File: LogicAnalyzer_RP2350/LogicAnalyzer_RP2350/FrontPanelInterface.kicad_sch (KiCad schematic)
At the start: 1 part, among them J1 874370843

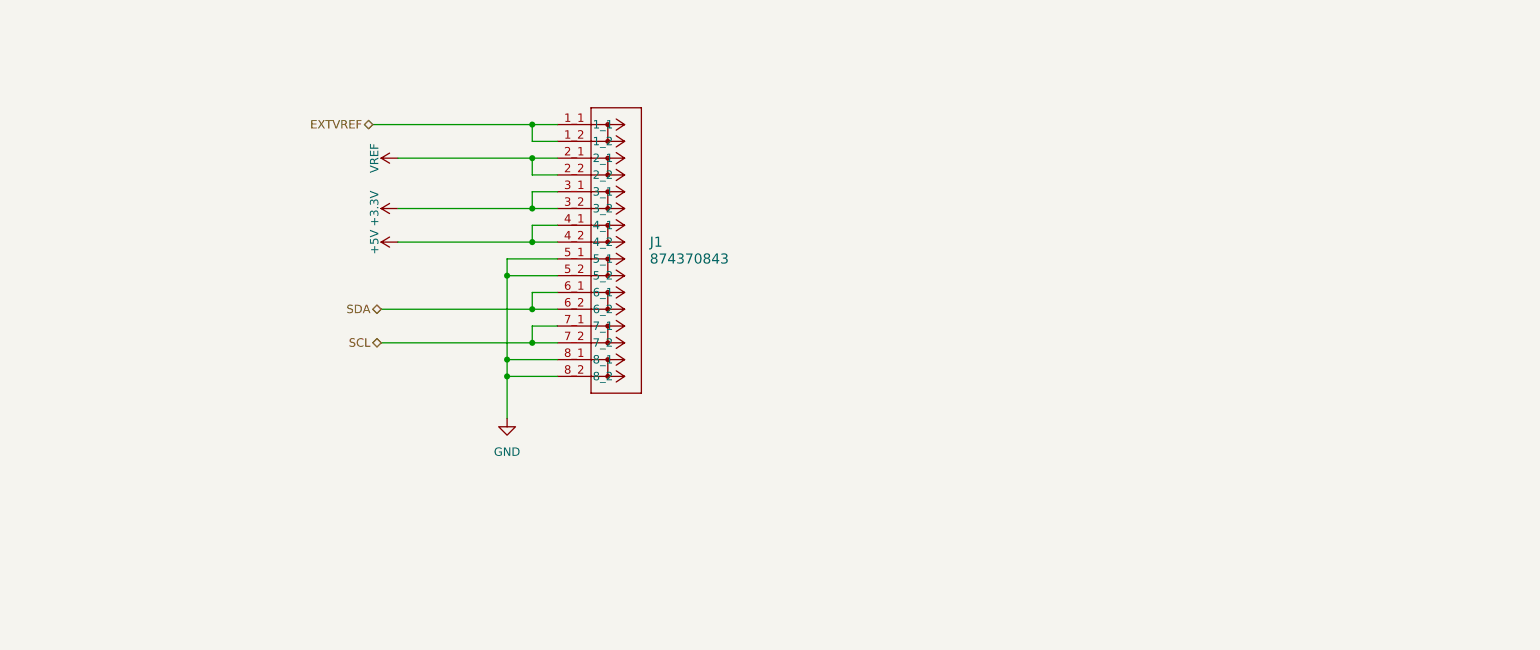
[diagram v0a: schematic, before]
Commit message: Added VMON Micro
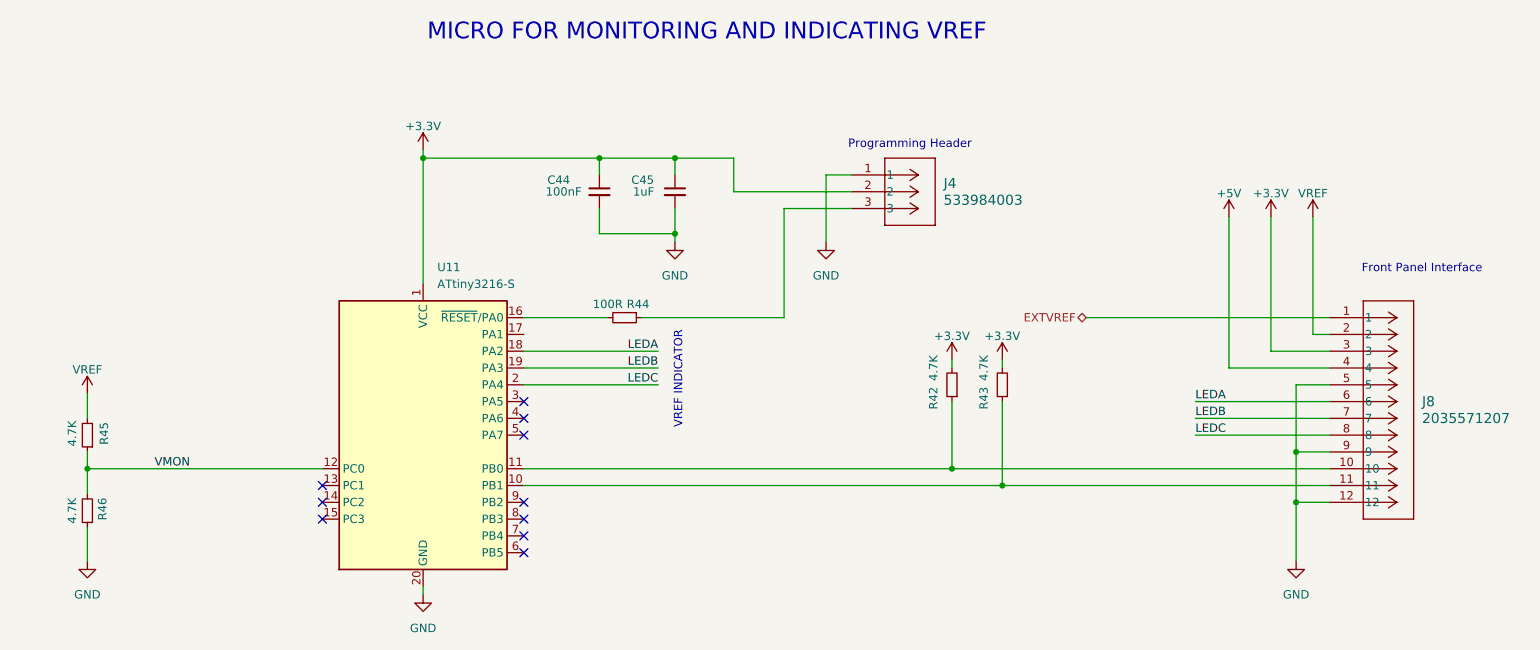
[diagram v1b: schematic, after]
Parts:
- removed J1: 874370843, CONN_874370231-SD_08_MOL, symbol Molex-874370843:874370843
- added C44: 100nF, Capacitor_SMD:C_0603_1608Metric_Pad1.08x0.95mm_HandSolder, symbol Device:C_Small
- added C45: 1uF, Capacitor_SMD:C_0603_1608Metric_Pad1.08x0.95mm_HandSolder, symbol Device:C_Small
- added J4: 533984003, CONN_533980002-SD_03_MOL, symbol Molex-533984003:533984003
- added J8: 2035571207, CONN_2035570000-SD_12_MOL, symbol Molex-2035571207:2035571207
- added R42, R43, R45, R46: 4.7K, Resistor_SMD:R_0603_1608Metric_Pad0.98x0.95mm_HandSolder, symbol Device:R_Small
- added R44: 100R, Resistor_SMD:R_0603_1608Metric_Pad0.98x0.95mm_HandSolder, symbol Device:R_Small
- added U11: ATtiny3216-S, Package_SO:SOIC-20W_7.5x12.8mm_P1.27mm, symbol MCU_Microchip_ATtiny:ATtiny3216-S
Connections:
- net +3.3V: now also C44.1, C45.1, J4.2, J8.3, R42.2, R43.2, U11.1 (VCC)
- net +5V: now also J8.4
- net EXTVREF: now also J8.1
- net GND: now also C44.2, C45.2, J4.1, J8.12, J8.5, J8.9, R46.1, U11.20 (GND)
- net VREF: now also J8.2, R45.2
- new net: J4.3, R44.1
- new net: R44.2, U11.16 (~{RESET}/PA0)
- new net: J8.11, R43.1, U11.10 (PB1)
- new net: J8.10, R42.1, U11.11 (PB0)
- new net LEDA: J8.6, U11.18 (PA2)
- new net LEDB: J8.7, U11.19 (PA3)
- new net LEDC: J8.8, U11.2 (PA4)
- new net VMON: R45.1, R46.2, U11.12 (PC0)
- no-connect marks 0 -> 10
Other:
- note added: "Front Panel Interface"
- note added: "MICRO FOR MONITORING AND INDICATING VREF"
- note added: "Programming Header"
- note added: "VREF INDICATOR"

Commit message: Clearing UP ERC Errors and Warnings
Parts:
- J4: footprint CONN_533980002-SD_03_MOL -> Molex-533984003:CONN_533980002-SD_03_MOL
- J8: footprint CONN_2035570000-SD_12_MOL -> Molex-2035571207:CONN_2035570000-SD_12_MOL
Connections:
- no-connect marks 10 -> 11
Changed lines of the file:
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@@
+	)
+	(no_connect
+		(at 110.49 91.44)
 	)
 	(no_connect
@@
 			)
 			(justify left bottom)
+		)
+	)
+	(hierarchical_label "VREF"
+		(shape output)
+		(at 44.45 100.33 90)
+		(effects
+			(font
+				(size 1.27 1.27)
+			)
+			(justify left)
+		)
+	)
+	(hierarchical_label "VREF"
+		(shape output)
+		(at 229.87 73.66 90)
+		(effects
+			(font
+				(size 1.27 1.27)
+			)
+			(justify left)
 		)
 	)
@@
 			)
 		)
-		(property "Footprint" "CONN_533980002-SD_03_MOL"
+		(property "Footprint" "Molex-533984003:CONN_533980002-SD_03_MOL"
 			(at 160.02 67.31 0)
 			(hide yes)
@@
 			)
 		)
-		(property "Footprint" "CONN_2035570000-SD_12_MOL"
+		(property "Footprint" "Molex-2035571207:CONN_2035570000-SD_12_MOL"
 			(at 232.41 88.9 0)
 			(hide yes)
@@
 	)
 	(symbol
-		(lib_id "power:+2V5")
-		(at 229.87 73.66 0)
-		(unit 1)
-		(body_style 1)
-		(exclude_from_sim no)
-		(in_bom yes)
-		(on_board yes)
-		(in_pos_files yes)
-		(dnp no)
-		(property "Reference" "#PWR0101"
-			(at 229.87 77.47 0)
-			(hide yes)
-			(show_name no)
-			(do_not_autoplace no)
-			(effects
-				(font
-					(size 1.27 1.27)
-				)
-			)
-		)
-		(property "Value" "VREF"
-			(at 229.87 70.104 0)
-			(show_name no)
-			(do_not_autoplace no)
-			(effects
-				(font
-					(size 1.27 1.27)
-				)
-			)
-		)
-		(property "Footprint" ""
-			(at 229.87 73.66 0)
-			(hide yes)
-			(show_name no)
-			(do_not_autoplace no)
-			(effects
-				(font
-					(size 1.27 1.27)
-				)
-			)
-		)
-		(property "Datasheet" ""
-			(at 229.87 73.66 0)
-			(hide yes)
-			(show_name no)
-			(do_not_autoplace no)
-			(effects
-				(font
-					(size 1.27 1.27)
-				)
-			)
-		)
-		(property "Description" "Power symbol creates a global label with name \"+2V5\""
-			(at 229.87 73.66 0)
-			(hide yes)
-			(show_name no)
-			(do_not_autoplace no)
-			(effects
-				(font
-					(size 1.27 1.27)
-				)
-			)
-		)
-		(pin "1"
-		)
-		(instances
-			(project "LogicAnalyzer_RP2350"
-				(path "/d75f24d0-99d8-459e-8e7b-473191ec3959/68c34580-4572-474c-bc8b-c0b67926a418"
-					(reference "#PWR0101")
-					(unit 1)
-				)
-			)
-		)
-	)
-	(symbol
 		(lib_id "Device:R_Small")
 		(at 44.45 106.68 180)
@@
 					(unit 1)
 				)
-			)
-		)
-	)
-	(symbol
-		(lib_id "power:+2V5")
-		(at 44.45 100.33 0)
-		(unit 1)
-		(body_style 1)
-		(exclude_from_sim no)
-		(in_bom yes)
-		(on_board yes)
-		(in_pos_files yes)
-		(dnp no)
-		(property "Reference" "#PWR0100"
-			(at 44.45 104.14 0)
-			(hide yes)
-			(show_name no)
-			(do_not_autoplace no)
-			(effects
-				(font
-					(size 1.27 1.27)
-				)
-			)
-		)
-		(property "Value" "VREF"
-			(at 44.45 96.774 0)
-			(show_name no)
-			(do_not_autoplace no)
-			(effects
-				(font
-					(size 1.27 1.27)
-				)
-			)
-		)
-		(property "Footprint" ""
-			(at 44.45 100.33 0)
-			(hide yes)
-			(show_name no)
-			(do_not_autoplace no)
-			(effects
-				(font
-					(size 1.27 1.27)
-				)
-			)
-		)
-		(property "Datasheet" ""
-			(at 44.45 100.33 0)
-			(hide yes)
-			(show_name no)
-			(do_not_autoplace no)
-			(effects
-				(font
-					(size 1.27 1.27)
-				)
-			)
-		)
-		(property "Description" "Power symbol creates a global label with name \"+2V5\""
-			(at 44.45 100.33 0)
-			(hide yes)
-			(show_name no)
-			(do_not_autoplace no)
-			(effects
-				(font
-					(size 1.27 1.27)
-				)
-			)
-		)
-		(pin "1"
-		)
-		(instances
-			(project "LogicAnalyzer_RP2350"
-				(path "/d75f24d0-99d8-459e-8e7b-473191ec3959/68c34580-4572-474c-bc8b-c0b67926a418"
-					(reference "#PWR0100")
-					(unit 1)
-				)

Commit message: Net Classes Added
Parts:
- renumbered C44 to C45, C45 to C46, J4 to J7, R44 to R47, R42 to R48, R43 to R49
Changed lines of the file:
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@@
 		(in_pos_files yes)
 		(dnp no)
-		(property "Reference" "#PWR096"
+		(property "Reference" "#PWR080"
 			(at 95.25 67.31 0)
 			(hide yes)
@@
 			(project "LogicAnalyzer_RP2350"
 				(path "/d75f24d0-99d8-459e-8e7b-473191ec3959/68c34580-4572-474c-bc8b-c0b67926a418"
-					(reference "#PWR096")
+					(reference "#PWR080")
 					(unit 1)
 				)
@@
 		(in_pos_files yes)
 		(dnp no)
-		(property "Reference" "#PWR0103"
+		(property "Reference" "#PWR086"
 			(at 217.17 77.47 0)
 			(hide yes)
@@
 			(project "LogicAnalyzer_RP2350"
 				(path "/d75f24d0-99d8-459e-8e7b-473191ec3959/68c34580-4572-474c-bc8b-c0b67926a418"
-					(reference "#PWR0103")
+					(reference "#PWR086")
 					(unit 1)
 				)
@@
 		(dnp no)
 		(fields_autoplaced yes)
-		(property "Reference" "#PWR087"
+		(property "Reference" "#PWR082"
 			(at 133.35 83.82 0)
 			(hide yes)
@@
 			(project "LogicAnalyzer_RP2350"
 				(path "/d75f24d0-99d8-459e-8e7b-473191ec3959/68c34580-4572-474c-bc8b-c0b67926a418"
-					(reference "#PWR087")
+					(reference "#PWR082")
 					(unit 1)
 				)
@@
 		(dnp no)
 		(fields_autoplaced yes)
-		(property "Reference" "#PWR088"
+		(property "Reference" "#PWR083"
 			(at 156.21 83.82 0)
 			(hide yes)
@@
 			(project "LogicAnalyzer_RP2350"
 				(path "/d75f24d0-99d8-459e-8e7b-473191ec3959/68c34580-4572-474c-bc8b-c0b67926a418"
-					(reference "#PWR088")
+					(reference "#PWR083")
 					(unit 1)
 				)
@@
 		(dnp no)
 		(fields_autoplaced yes)
-		(property "Reference" "#PWR0104"
+		(property "Reference" "#PWR088"
 			(at 227.33 132.08 0)
 			(hide yes)
@@
 			(project "LogicAnalyzer_RP2350"
 				(path "/d75f24d0-99d8-459e-8e7b-473191ec3959/68c34580-4572-474c-bc8b-c0b67926a418"
-					(reference "#PWR0104")
+					(reference "#PWR088")
 					(unit 1)
 				)
@@
 		(in_pos_files yes)
 		(dnp no)
-		(property "Reference" "C44"
+		(property "Reference" "C45"
 			(at 114.046 68.072 0)
 			(show_name no)
@@
 			(project "LogicAnalyzer_RP2350"
 				(path "/d75f24d0-99d8-459e-8e7b-473191ec3959/68c34580-4572-474c-bc8b-c0b67926a418"
-					(reference "C44")
+					(reference "C45")
 					(unit 1)
 				)
@@
 		(in_pos_files yes)
 		(dnp no)
-		(property "Reference" "R44"
+		(property "Reference" "R47"
 			(at 127.762 86.868 90)
 			(show_name no)
@@
 			(project "LogicAnalyzer_RP2350"
 				(path "/d75f24d0-99d8-459e-8e7b-473191ec3959/68c34580-4572-474c-bc8b-c0b67926a418"
-					(reference "R44")
+					(reference "R47")
 					(unit 1)
 				)
@@
 		(in_pos_files yes)
 		(dnp no)
-		(property "Reference" "#PWR097"
+		(property "Reference" "#PWR084"
 			(at 175.26 99.06 0)
 			(hide yes)
@@
 			(project "LogicAnalyzer_RP2350"
 				(path "/d75f24d0-99d8-459e-8e7b-473191ec3959/68c34580-4572-474c-bc8b-c0b67926a418"
-					(reference "#PWR097")
+					(reference "#PWR084")
 					(unit 1)
 				)
@@
 		(dnp no)
 		(fields_autoplaced yes)
-		(property "Reference" "#PWR090"
+		(property "Reference" "#PWR079"
 			(at 44.45 132.08 0)
 			(hide yes)
@@
 			(project "LogicAnalyzer_RP2350"
 				(path "/d75f24d0-99d8-459e-8e7b-473191ec3959/68c34580-4572-474c-bc8b-c0b67926a418"
-					(reference "#PWR090")
+					(reference "#PWR079")
 					(unit 1)
 				)
@@
 		(dnp no)
 		(fields_autoplaced yes)
-		(property "Reference" "#PWR099"
+		(property "Reference" "#PWR081"
 			(at 95.25 137.16 0)
 			(hide yes)
@@
 			(project "LogicAnalyzer_RP2350"
 				(path "/d75f24d0-99d8-459e-8e7b-473191ec3959/68c34580-4572-474c-bc8b-c0b67926a418"
-					(reference "#PWR099")
+					(reference "#PWR081")
 					(unit 1)
 				)
@@
 		(in_pos_files yes)
 		(dnp no)
-		(property "Reference" "C45"
+		(property "Reference" "C46"
 			(at 126.746 68.072 0)
 			(show_name no)
@@
 			(project "LogicAnalyzer_RP2350"
 				(path "/d75f24d0-99d8-459e-8e7b-473191ec3959/68c34580-4572-474c-bc8b-c0b67926a418"
-					(reference "C45")
+					(reference "C46")
 					(unit 1)
 				)
@@
 		(dnp no)
 		(fields_autoplaced yes)
-		(property "Reference" "J4"
+		(property "Reference" "J7"
 			(at 173.99 68.5799 0)
 			(show_name no)
@@
 			(project "LogicAnalyzer_RP2350"
 				(path "/d75f24d0-99d8-459e-8e7b-473191ec3959/68c34580-4572-474c-bc8b-c0b67926a418"
-					(reference "J4")
+					(reference "J7")
 					(unit 1)
 				)
@@
 		(in_pos_files yes)
 		(dnp no)
-		(property "Reference" "R43"
+		(property "Reference" "R49"
 			(at 180.086 101.092 90)
 			(show_name no)
@@
 			(project "LogicAnalyzer_RP2350"
 				(path "/d75f24d0-99d8-459e-8e7b-473191ec3959/68c34580-4572-474c-bc8b-c0b67926a418"
-					(reference "R43")
+					(reference "R49")
 					(unit 1)
 				)
@@
 		(in_pos_files yes)
 		(dnp no)
-		(property "Reference" "R42"
+		(property "Reference" "R48"
 			(at 172.466 101.092 90)
 			(show_name no)
@@
 			(project "LogicAnalyzer_RP2350"
 				(path "/d75f24d0-99d8-459e-8e7b-473191ec3959/68c34580-4572-474c-bc8b-c0b67926a418"
-					(reference "R42")
+					(reference "R48")
 					(unit 1)
 				)
@@
 		(in_pos_files yes)
 		(dnp no)
-		(property "Reference" "#PWR0102"
+		(property "Reference" "#PWR087"
 			(at 223.52 77.47 0)
 			(hide yes)
@@
 			(project "LogicAnalyzer_RP2350"
 				(path "/d75f24d0-99d8-459e-8e7b-473191ec3959/68c34580-4572-474c-bc8b-c0b67926a418"
-					(reference "#PWR0102")
+					(reference "#PWR087")
 					(unit 1)
 				)
@@
 		(in_pos_files yes)
 		(dnp no)
-		(property "Reference" "#PWR098"
+		(property "Reference" "#PWR085"
 			(at 182.88 99.06 0)
 			(hide yes)
@@
 			(project "LogicAnalyzer_RP2350"
 				(path "/d75f24d0-99d8-459e-8e7b-473191ec3959/68c34580-4572-474c-bc8b-c0b67926a418"
-					(reference "#PWR098")
-					(unit 1)
-				)
+					(reference "#PWR085")
+					(unit 1)
+				)

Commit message: Added Missing 3D Models
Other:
- moved on the sheet: C45, C46, J7, J8, R45, R46, R47, R48, R49, U11
